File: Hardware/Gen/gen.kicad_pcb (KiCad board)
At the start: 2 copper layers, 149.8 x 65.8 mm, 54 parts, among them J1 Screw_Terminal_01x03, J2 XLR4, J3 XLR3, J4 GAMEN, J5 SHORI, J6 MAE, J7 Screw_Terminal_01x02, U1 TPS56339DDCT, U3 TPS560430YDBVR

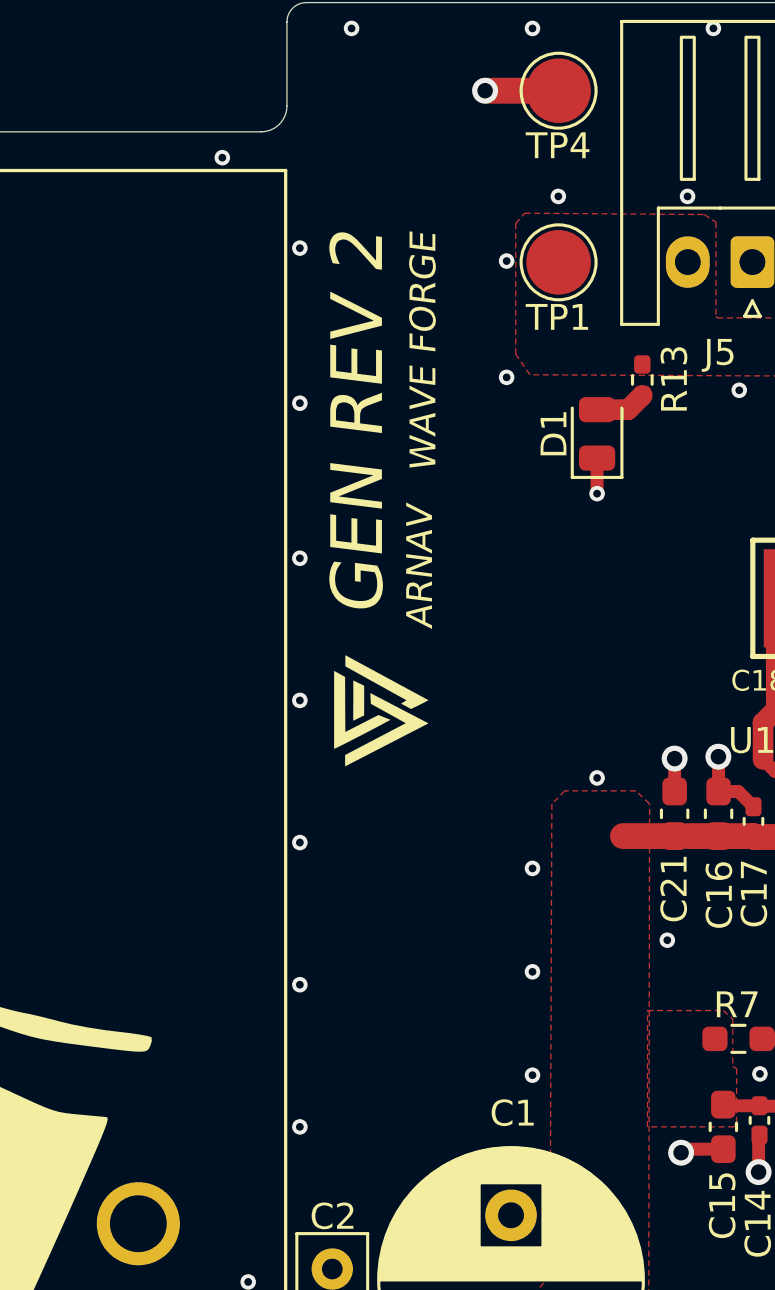
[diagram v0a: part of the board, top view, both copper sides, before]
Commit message: Gen: 5V buck convertor rework schems
Changed the 5V buck convertor to fgollow a ti chip with more of a max voltage headroom for safety.
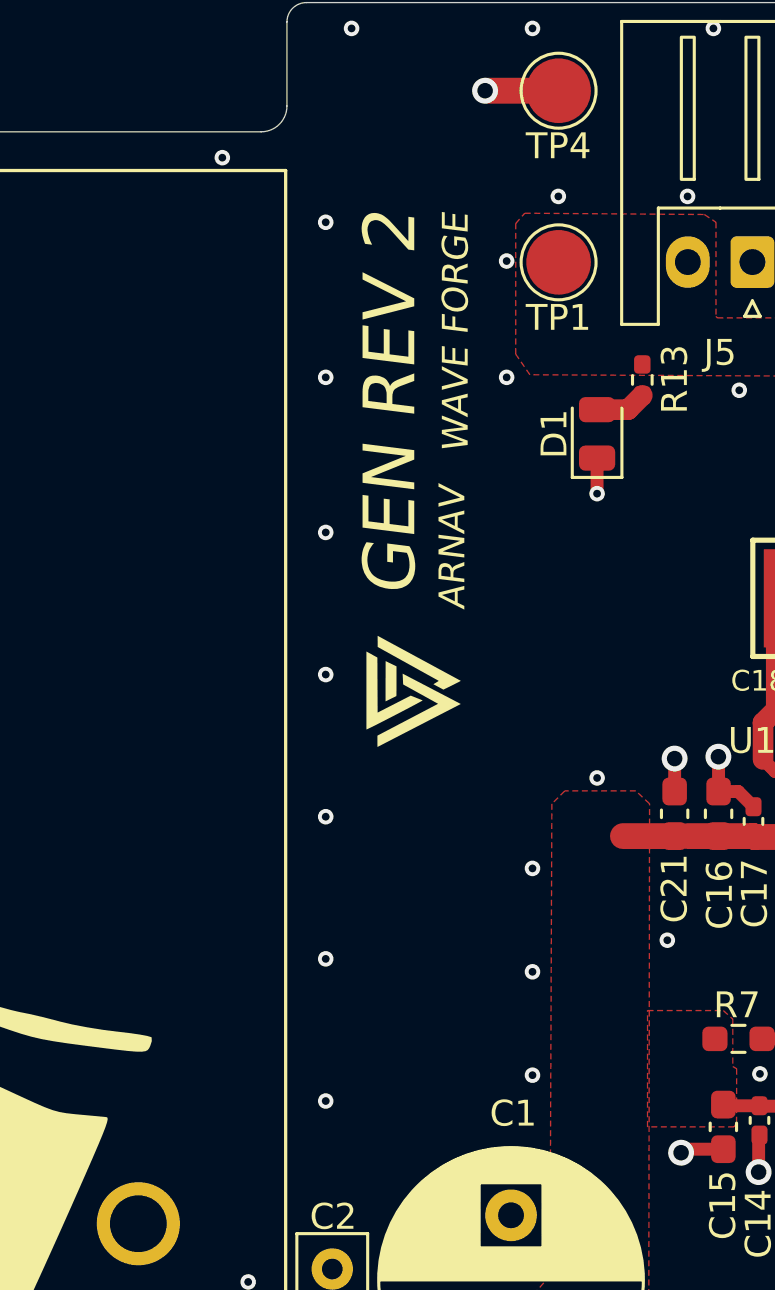
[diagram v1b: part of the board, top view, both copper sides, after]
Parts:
- moved G*** 1.46 mm to (176.3, 107.9)

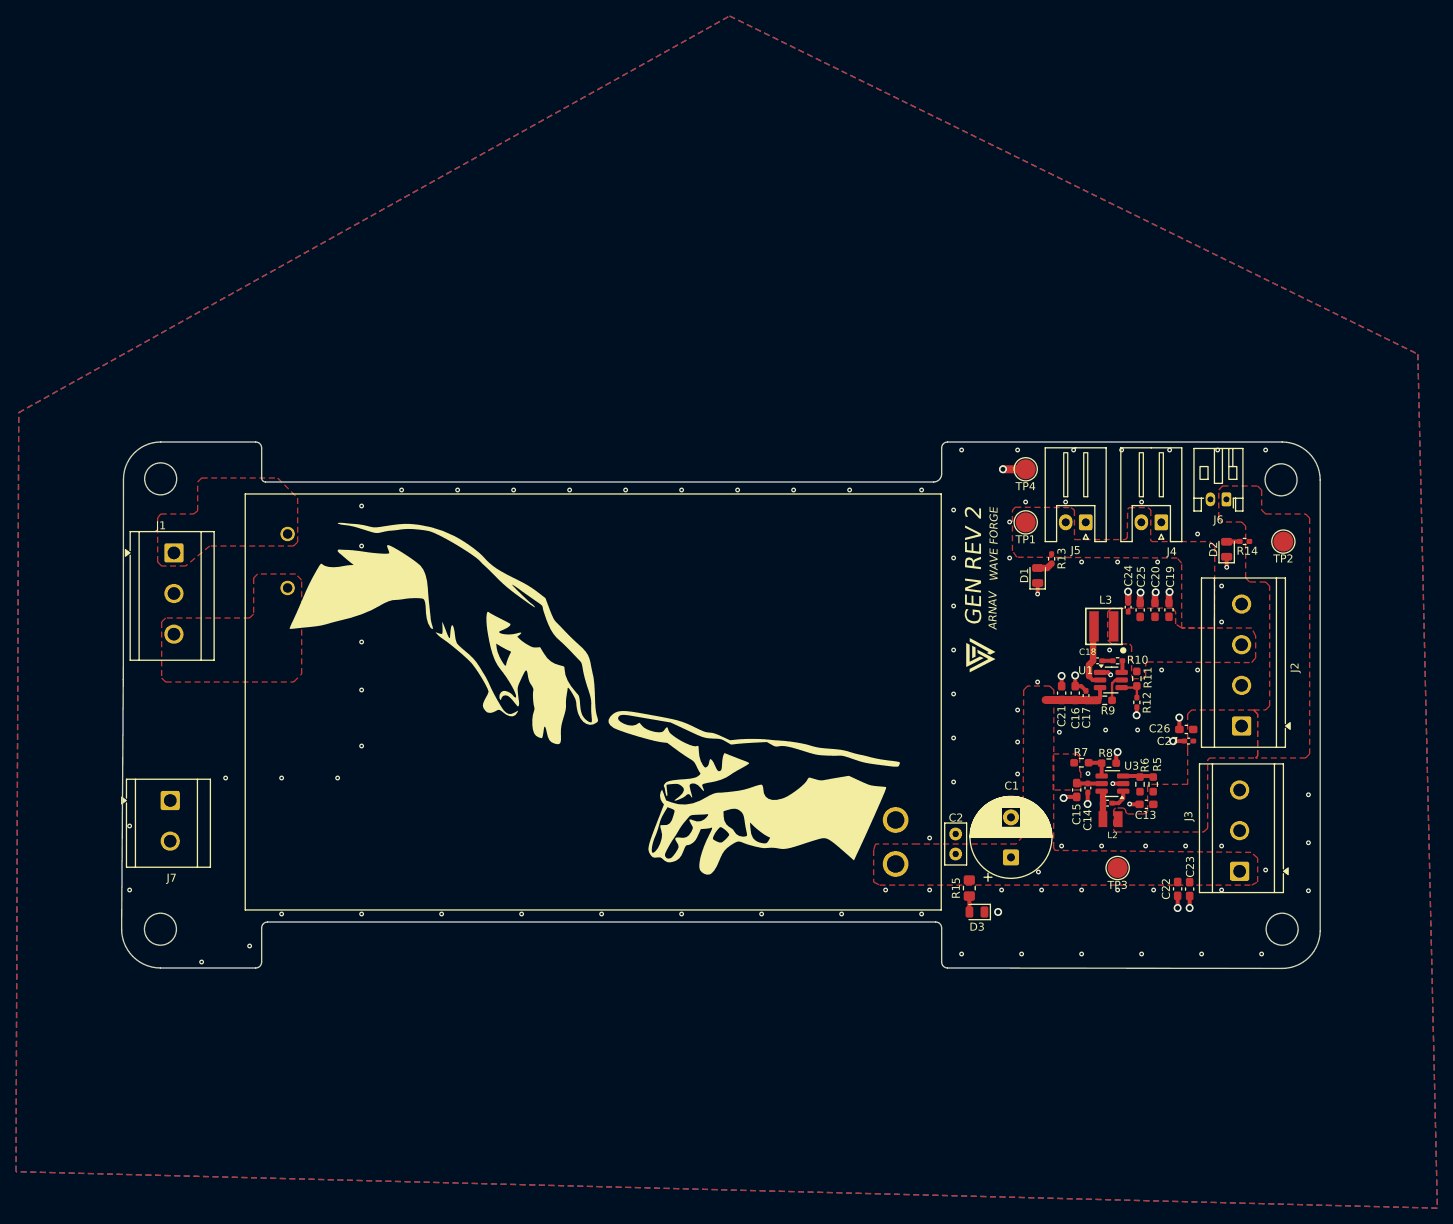
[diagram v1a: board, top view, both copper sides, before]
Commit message: Gen: Barrel Jack Or-ing Circuit, and cart made
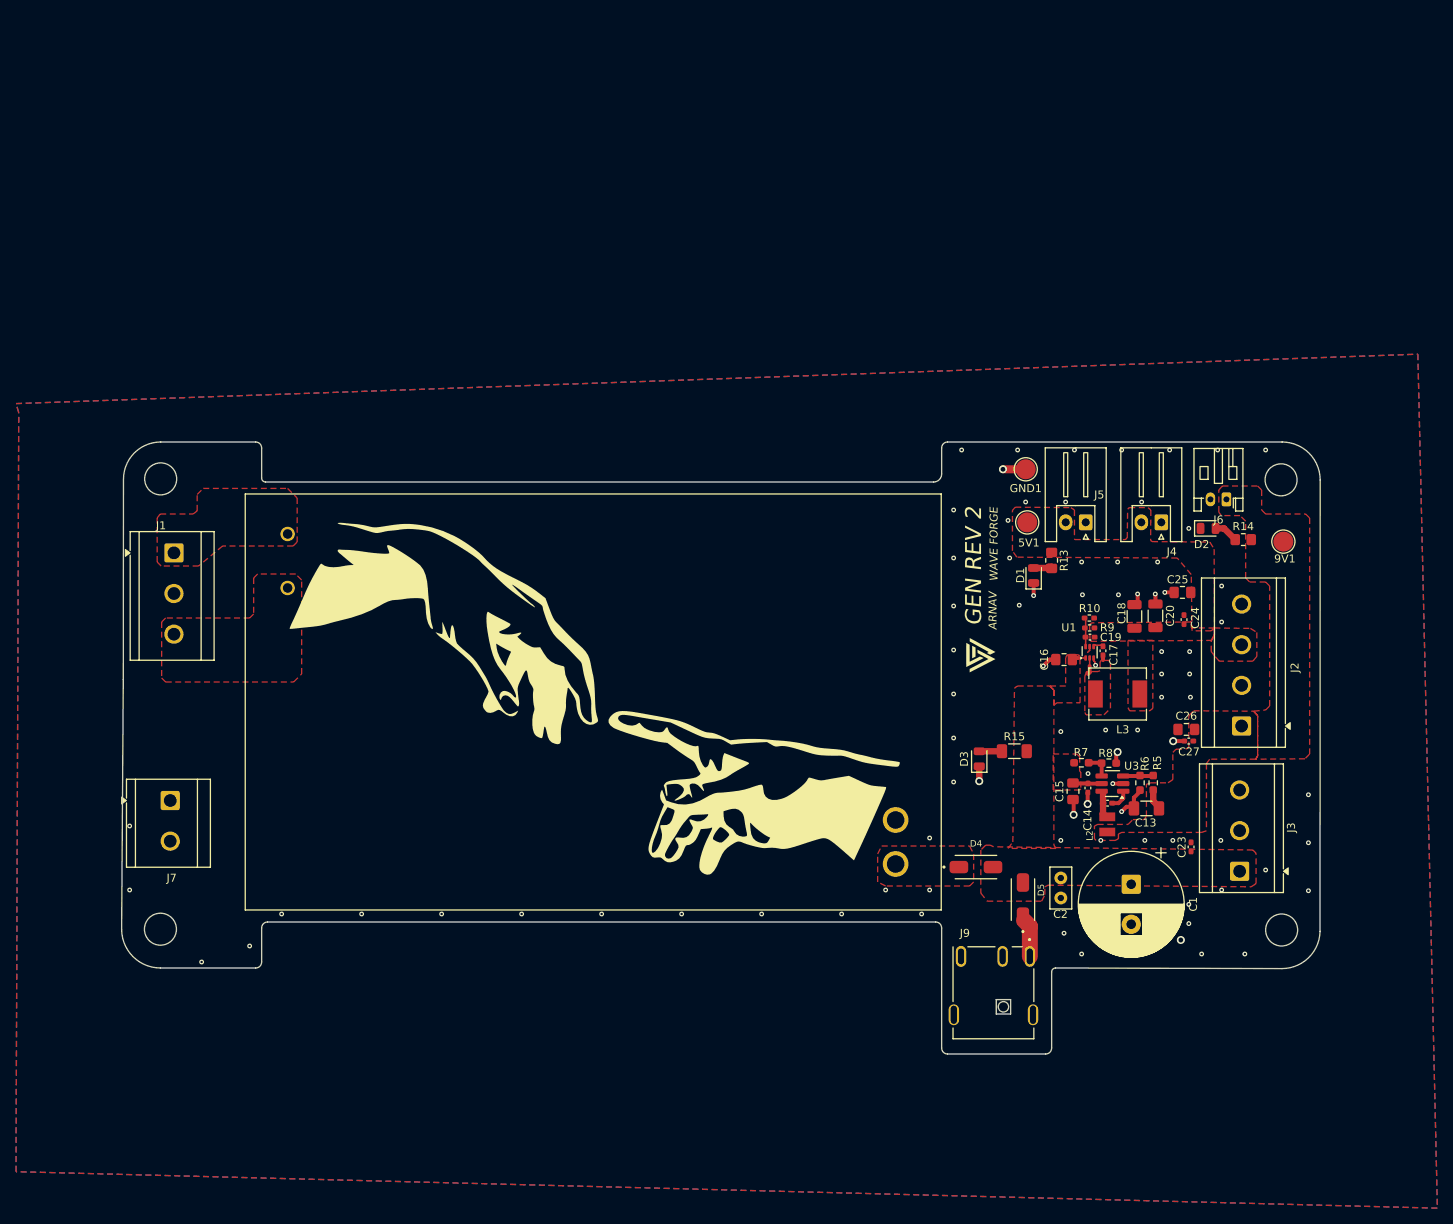
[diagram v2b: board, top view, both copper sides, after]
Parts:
- removed C21, C22: 10uF, Capacitor_SMD:C_0603_1608Metric_Pad1.08x0.95mm_HandSolder
- removed R11: 52.3K, Resistor_SMD:R_0603_1608Metric_Pad0.98x0.95mm_HandSolder
- removed R12: 10K, Resistor_SMD:R_0402_1005Metric_Pad0.72x0.64mm_HandSolder
- removed TP3: TestPoint, TestPoint:TestPoint_Pad_D2.5mm
- added D4: B340, My FeetPics:DIOM5226X240N, F.Cu at (176.8, 134.1)
- added D5: B340, My FeetPics:DIOM5226X240N, F.Cu at (182.7, 138.2)
- added J9: PJ-051A, My FeetPics:CUI_PJ-051A, F.Cu at (179.0, 149.8)
- C1: footprint Capacitor_THT:CP_Radial_D10.0mm_P5.00mm -> Capacitor_THT:CP_Radial_D13.0mm_P5.00mm
- C13: footprint Capacitor_SMD:C_0603_1608Metric_Pad1.08x0.95mm_HandSolder -> Capacitor_SMD:C_1206_3216Metric_Pad1.33x1.80mm_HandSolder
- C15, C25, C26: footprint Capacitor_SMD:C_0603_1608Metric_Pad1.08x0.95mm_HandSolder -> Capacitor_SMD:C_0805_2012Metric_Pad1.18x1.45mm_HandSolder
- C16: value 10uF -> 3.3uF; footprint Capacitor_SMD:C_0603_1608Metric_Pad1.08x0.95mm_HandSolder -> Capacitor_SMD:C_0805_2012Metric_Pad1.18x1.45mm_HandSolder
- C18: value 100nF -> 47uF; footprint Capacitor_SMD:C_0402_1005Metric_Pad0.74x0.62mm_HandSolder -> Capacitor_SMD:C_1206_3216Metric
- C19: value 22uF -> 82pF; footprint Capacitor_SMD:C_0603_1608Metric_Pad1.08x0.95mm_HandSolder -> Capacitor_SMD:C_0402_1005Metric_Pad0.74x0.62mm_HandSolder
- C20: value 22uF -> 47uF; footprint Capacitor_SMD:C_0603_1608Metric_Pad1.08x0.95mm_HandSolder -> Capacitor_SMD:C_1206_3216Metric
- C23: footprint Capacitor_SMD:C_0603_1608Metric_Pad1.08x0.95mm_HandSolder -> Capacitor_SMD:C_0402_1005Metric_Pad0.74x0.62mm_HandSolder
- L3: value 5.6uH -> 10uH; footprint My footprints:WE-XHMI_4040 -> My Footprints:IND_SRP6540-100M
- R10: value 30 -> 13.7K
- R13, R14: footprint Resistor_SMD:R_0402_1005Metric_Pad0.72x0.64mm_HandSolder -> Resistor_SMD:R_0805_2012Metric_Pad1.20x1.40mm_HandSolder
- R15: footprint Resistor_SMD:R_0805_2012Metric_Pad1.20x1.40mm_HandSolder -> Resistor_SMD:R_1206_3216Metric_Pad1.30x1.75mm_HandSolder
- R9: footprint Resistor_SMD:R_0603_1608Metric_Pad0.98x0.95mm_HandSolder -> Resistor_SMD:R_0402_1005Metric_Pad0.72x0.64mm_HandSolder
- U1: value TPS56339DDCT -> TPS543021DRLR; footprint Package_TO_SOT_SMD:SOT-23-6_Handsoldering -> Package_TO_SOT_SMD:SOT-563
- moved D3 19.2 mm to (177.2, 120.6), turned to 90 degrees
- moved R15 18.0 mm to (181.6, 119.7), turned to 0 degrees
- moved C1 15.4 mm to (196.2, 136.3), turned to -90 degrees
- moved C2 13.5 mm to (187.4, 135.5), turned to -90 degrees
- moved C19 10.4 mm to (191.0, 105.4), turned to 180 degrees
- moved R9 9.24 mm to (191.0, 104.2), turned to 180 degrees
- moved L3 8.62 mm to (194.5, 112.5), turned to 180 degrees
- moved C18 7.21 mm to (196.6, 102.8), turned to -90 degrees
- moved C24 7.16 mm to (202.8, 103.2)
- moved R10 6.41 mm to (191.0, 103.0), turned to 0 degrees
- moved C17 5.97 mm to (192.7, 107.1), turned to 90 degrees
- moved C25 5.72 mm to (202.6, 99.8), turned to 0 degrees
- moved C23 5.27 mm to (203.7, 131.6), turned to -90 degrees
- moved C16 4.42 mm to (187.8, 108.2), turned to 0 degrees
- moved U1 4.36 mm to (191.0, 107.3), turned to 90 degrees
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- renumbered TP1 to 5V1, TP2 to 9V1, TP4 to GND1
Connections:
- C17 pad 1: GND -> Net-(U1-SW)
- C17 pad 2: /DC_OUT -> Net-(U1-BOOT)
- C18 pad 1: Net-(U1-SW) -> GND
- C18 pad 2: Net-(C18-Pad2) -> +5V
- C19 pad 1: GND -> +5V
- C19 pad 2: +5V -> Net-(U1-FB)
- PS1 pad +VO: /DC_OUT -> Net-(D4-A)
- R10 pad 1: Net-(U1-BOOT) -> Net-(U1-FB)
- R10 pad 2: Net-(C18-Pad2) -> GND
- R9 pad 1: /DC_OUT -> +5V
- R9 pad 2: Net-(U1-EN) -> Net-(U1-FB)
- U1 pad 1: GND -> /DC_OUT
- U1 pad 3: /DC_OUT -> GND
- U1 pad 4: Net-(U1-FB) -> Net-(U1-BOOT)
- U1 pad 5: Net-(U1-EN) -> unconnected-(U1-EN-Pad5)
- U1 pad 6: Net-(U1-BOOT) -> Net-(U1-FB)
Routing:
- net GND: track 30.6 -> 24.6 mm, vias 113 -> 87
- net /DC_OUT: track 10.9 -> 4.89 mm
- net Net-(U1-SW): track 8.07 -> 2.68 mm
- net Net-(D5-A): track 0.00 -> 4.80 mm
- net Net-(U1-EN): track 3.49 -> 0.00 mm
- net +9V: track 0.00 -> 2.38 mm
- net Net-(D2-A): track 1.67 -> 3.04 mm
- net Net-(C18-Pad2): track 1.34 -> 0.00 mm
- net Net-(D3-A): track 2.00 -> 2.86 mm
- net unconnected-(U1-EN-Pad5): track 0.00 -> 0.81 mm
- net Net-(D1-A): track 1.98 -> 2.71 mm
- added copper zone on F.Cu, net Net-(D4-A)
- added copper zone on F.Cu, net Net-(U1-SW)
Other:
- board size 149.8 x 65.8 mm -> 149.8 x 76.5 mm

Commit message: added stiching vias on gen and changed SWD header on shori to header pins
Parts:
- removed J9: PJ-051A, My FeetPics:CUI_PJ-051A
- added J8: PJ-063BH, My FeetPics:CUI_PJ-063BH, F.Cu at (179.5, 144.5)
- R9: value 100K -> 107K
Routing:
- net Net-(D5-A): track 4.80 -> 5.45 mm
